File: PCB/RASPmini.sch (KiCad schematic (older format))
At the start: 14 parts, among them P0 Raspberry PI GPIO, P1 MPU9250, P2 MS5611, P3 PCA9685, P5 UART, P6 RC INPUT

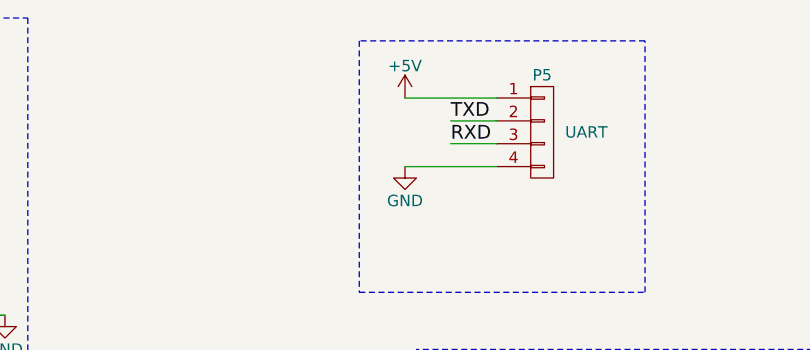
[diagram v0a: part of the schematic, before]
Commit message: 串口电源改为3.3v
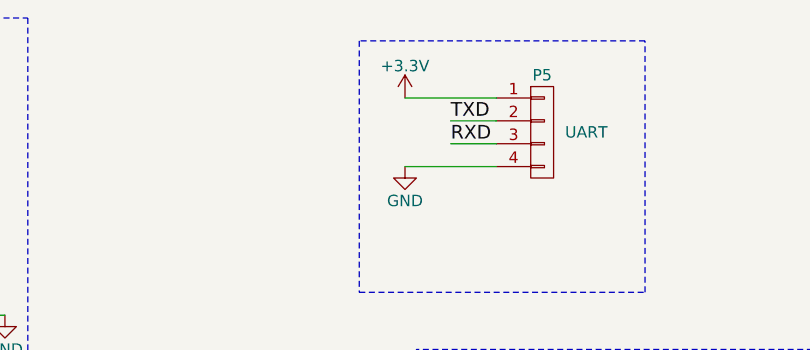
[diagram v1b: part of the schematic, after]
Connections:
- net +3V3: now also P5.1 (P1)
- net +5V: no longer P5.1 (P1)
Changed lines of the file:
@@
 LIBS:contrib
 LIBS:valves
-LIBS:Pxfmini-cache
+LIBS:RASPmini-cache
 EELAYER 25 0
 EELAYER END
@@
 	1    0    0    -1
 $EndComp
-$Comp
-L +5V #PWR013
-U 1 1 57EE9579
-P 5150 1100
-F 0 "#PWR013" H 5150 950 50  0001 C CNN
-F 1 "+5V" H 5150 1240 50  0000 C CNN
-F 2 "" H 5150 1100 50  0000 C CNN
-F 3 "" H 5150 1100 50  0000 C CNN
-	1    5150 1100
-	1    0    0    -1
-$EndComp
 Text Label 5350 1200 0    60   ~ 0
 TXD
@@
 Wire Wire Line
 	2000 1350 1450 1350
+$Comp
+L +3.3V #PWR?
+U 1 1 58081D74
+P 5150 1100
+F 0 "#PWR?" H 5150 950 50  0001 C CNN
+F 1 "+3.3V" H 5150 1240 50  0000 C CNN
+F 2 "" H 5150 1100 50  0000 C CNN
+F 3 "" H 5150 1100 50  0000 C CNN
+	1    5150 1100
+	1    0    0    -1
+$EndComp
 $EndSCHEMATC
